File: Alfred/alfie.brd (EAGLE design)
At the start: 85.2 x 46.3 mm, 33 parts, among them IC1 7805TV, K1 G6A-234P, K2 G6A-234P

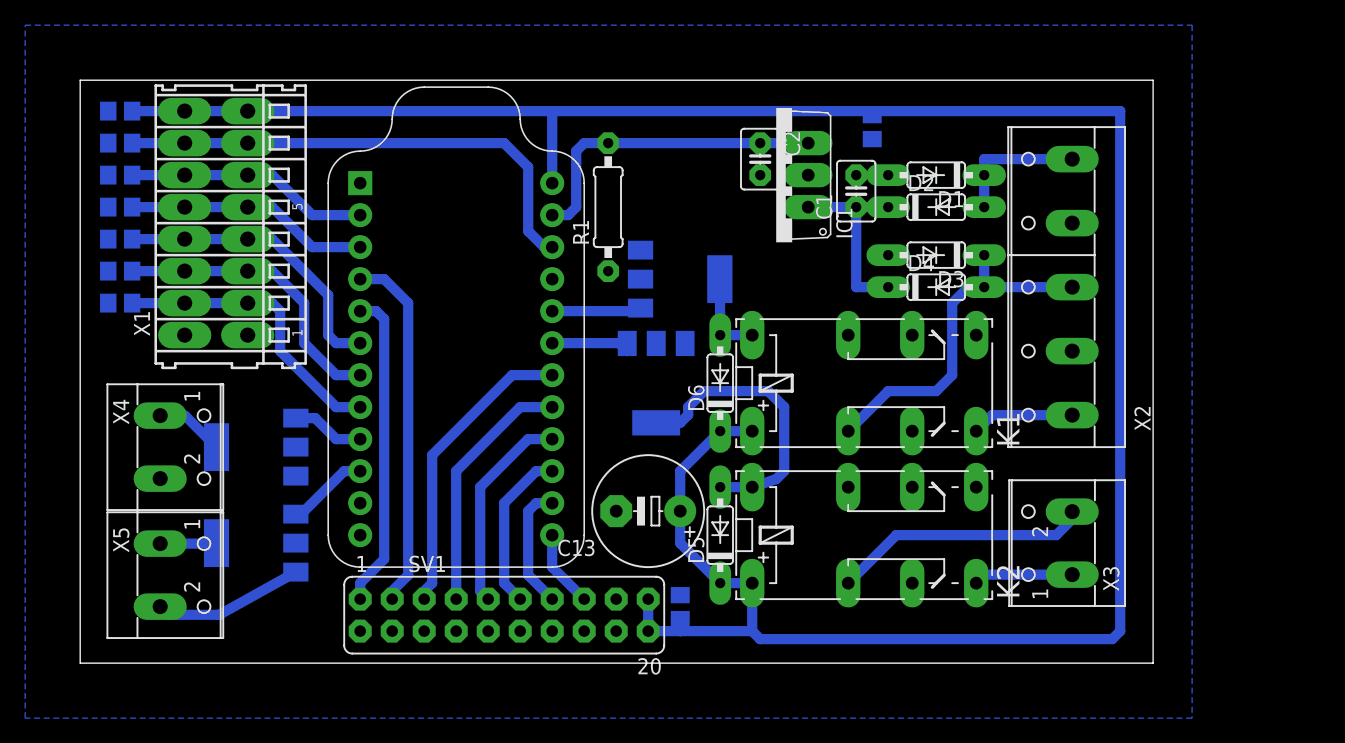
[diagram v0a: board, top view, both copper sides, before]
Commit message: Applied bjdooks patches to bring this to the board as etched.
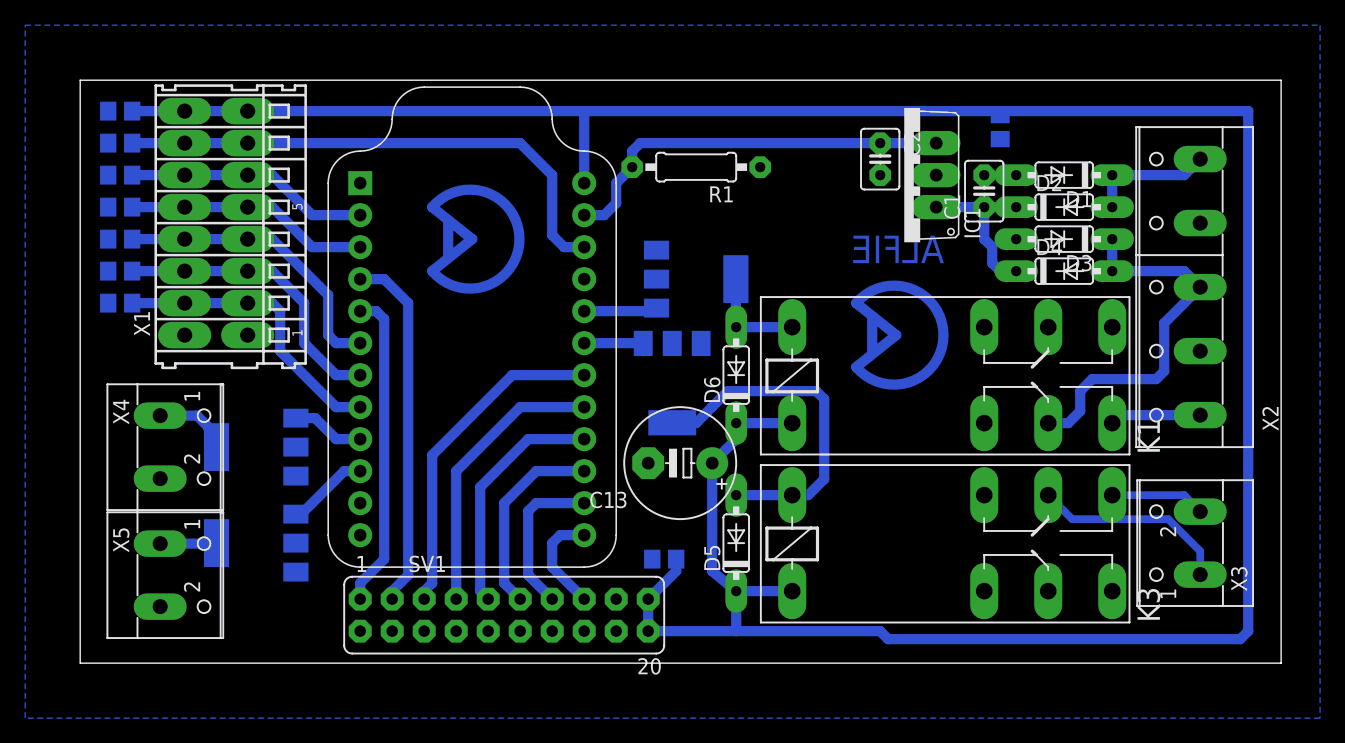
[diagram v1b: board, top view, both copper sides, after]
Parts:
- removed K2: G6A-234P, relay:G6A-234P
- added K3: 4052, relay:F4052
- K1: value G6A-234P -> 4052; device relay:G6A-234P -> relay:F4052
- moved D3 10.2 mm to (77.5, 33.0)
- moved D4 10.2 mm to (77.5, 30.5)
- moved X3 10.2 mm to (87.0, 8.89)
- moved C1 10.2 mm to (71.1, 36.8)
- moved C10 10.2 mm to (72.4, 41.9)
- moved D1 10.2 mm to (77.5, 38.1)
- moved D2 10.2 mm to (77.5, 35.6)
- moved IC1 10.2 mm to (64.8, 38.1)
- moved X2 10.2 mm to (87.6, 29.2)
- moved C2 9.52 mm to (62.9, 39.4)
- moved R1 7.67 mm to (48.3, 38.7), turned to 180 degrees
- moved C13 4.58 mm to (47.0, 15.2)
- moved C11 4.02 mm to (45.7, 7.62), turned to 0 degrees
- moved K1 3.24 mm to (59.7, 22.2)
- moved D6 1.42 mm to (51.4, 22.2)
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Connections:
- removed net N$7: K2.P1, X3.2
- new net N$6: K3.S2, X3.2
- net +5V: now also K1.2, K3.2; no longer K1.1, K2.1
- net N$1: now also K1.1; no longer K1.16
- net N$2: now also K3.1; no longer K2.16
- net N$4: now also K3.P2; no longer K2.S1
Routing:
- net +5V: track 190.8 -> 217.8 mm
- net N$10: track 0.00 -> 13.2 mm
- net GND: track 11.9 -> 0.00 mm
- net N$6: track 0.00 -> 7.55 mm
- net N$4: track 8.26 -> 15.8 mm
- net N$7: track 20.5 -> 13.2 mm
- net DOORBELL: track 25.3 -> 32.0 mm
- net N$2: track 22.6 -> 27.2 mm
- net N$1: track 6.99 -> 9.58 mm
- net N$11: track 0.00 -> 2.54 mm
- net N$9: track 0.00 -> 2.54 mm
- net IO_5: track 9.94 -> 12.5 mm
- net IO_4: track 13.0 -> 15.5 mm
- net IO_3: track 16.4 -> 19.0 mm
- net IO_2: track 19.9 -> 22.4 mm
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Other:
- board size 85.2 x 46.3 mm -> 95.3 x 46.3 mm
- board text added: "ALFIE"
